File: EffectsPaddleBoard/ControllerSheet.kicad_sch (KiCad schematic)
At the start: 21 parts, among them J1 Conn_01x03_Pin, J2 Conn_01x06_Pin, J4 Conn_01x04_Pin, SW1 SW_SPDT, SW2 SW_SPDT, SW3 SW_SPDT, U1 STM32F405RGTx, Y1 16MHz

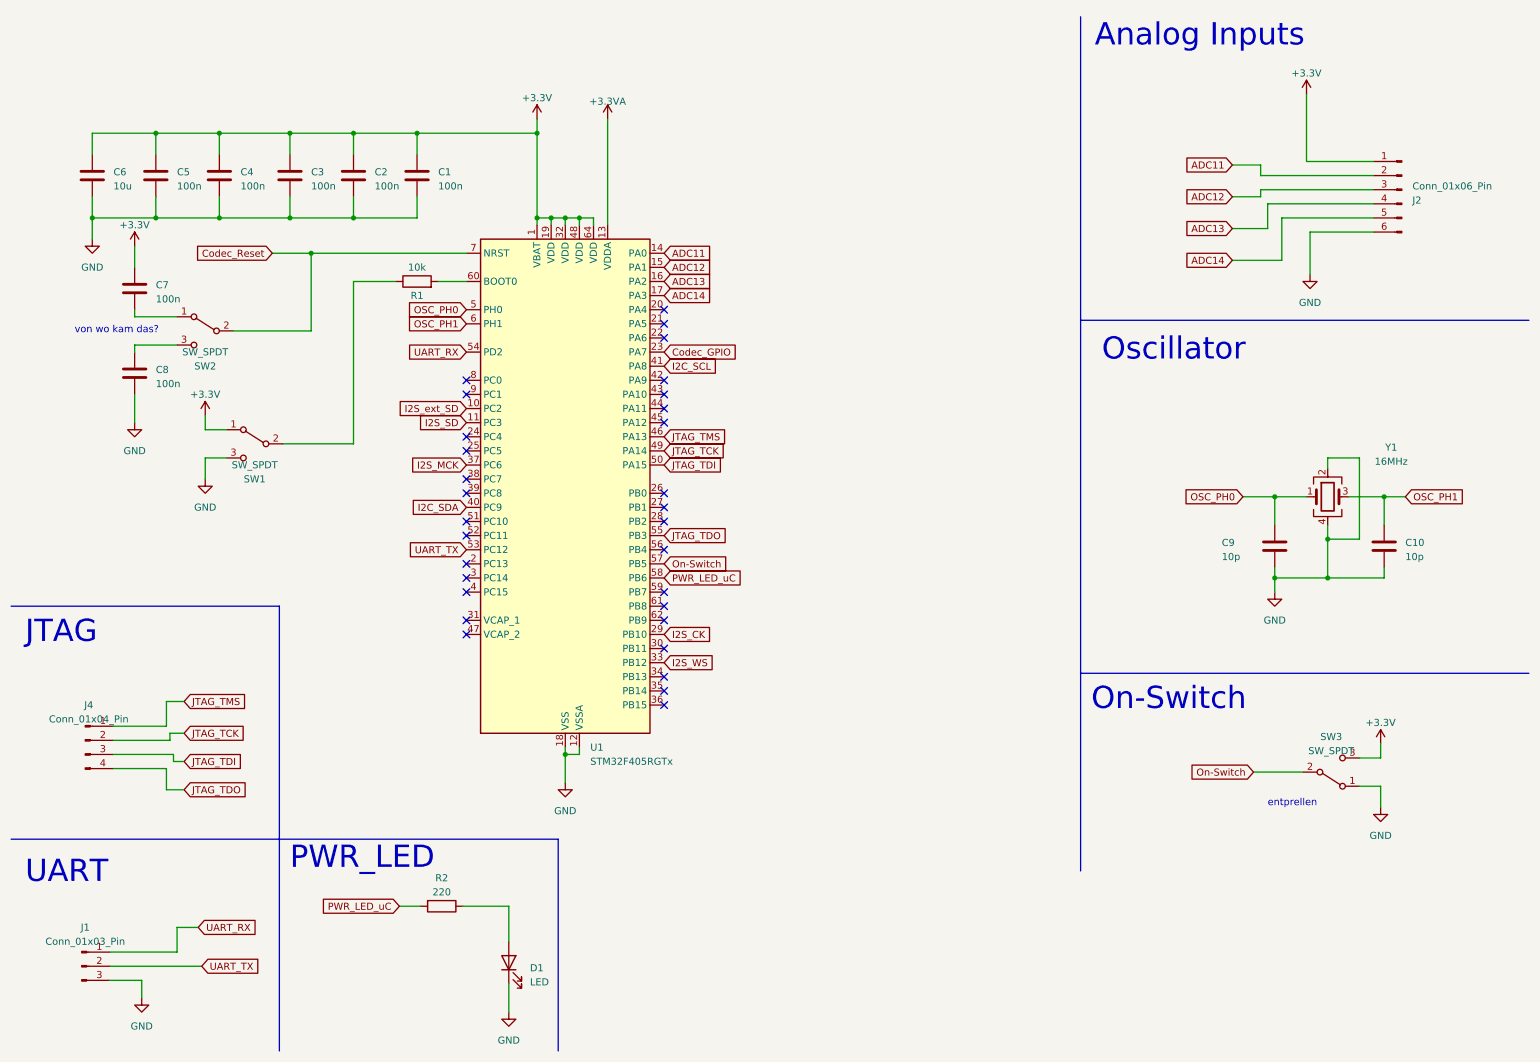
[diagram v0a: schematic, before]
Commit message: Added netclass colours and basic routing, made small changes in reset structure
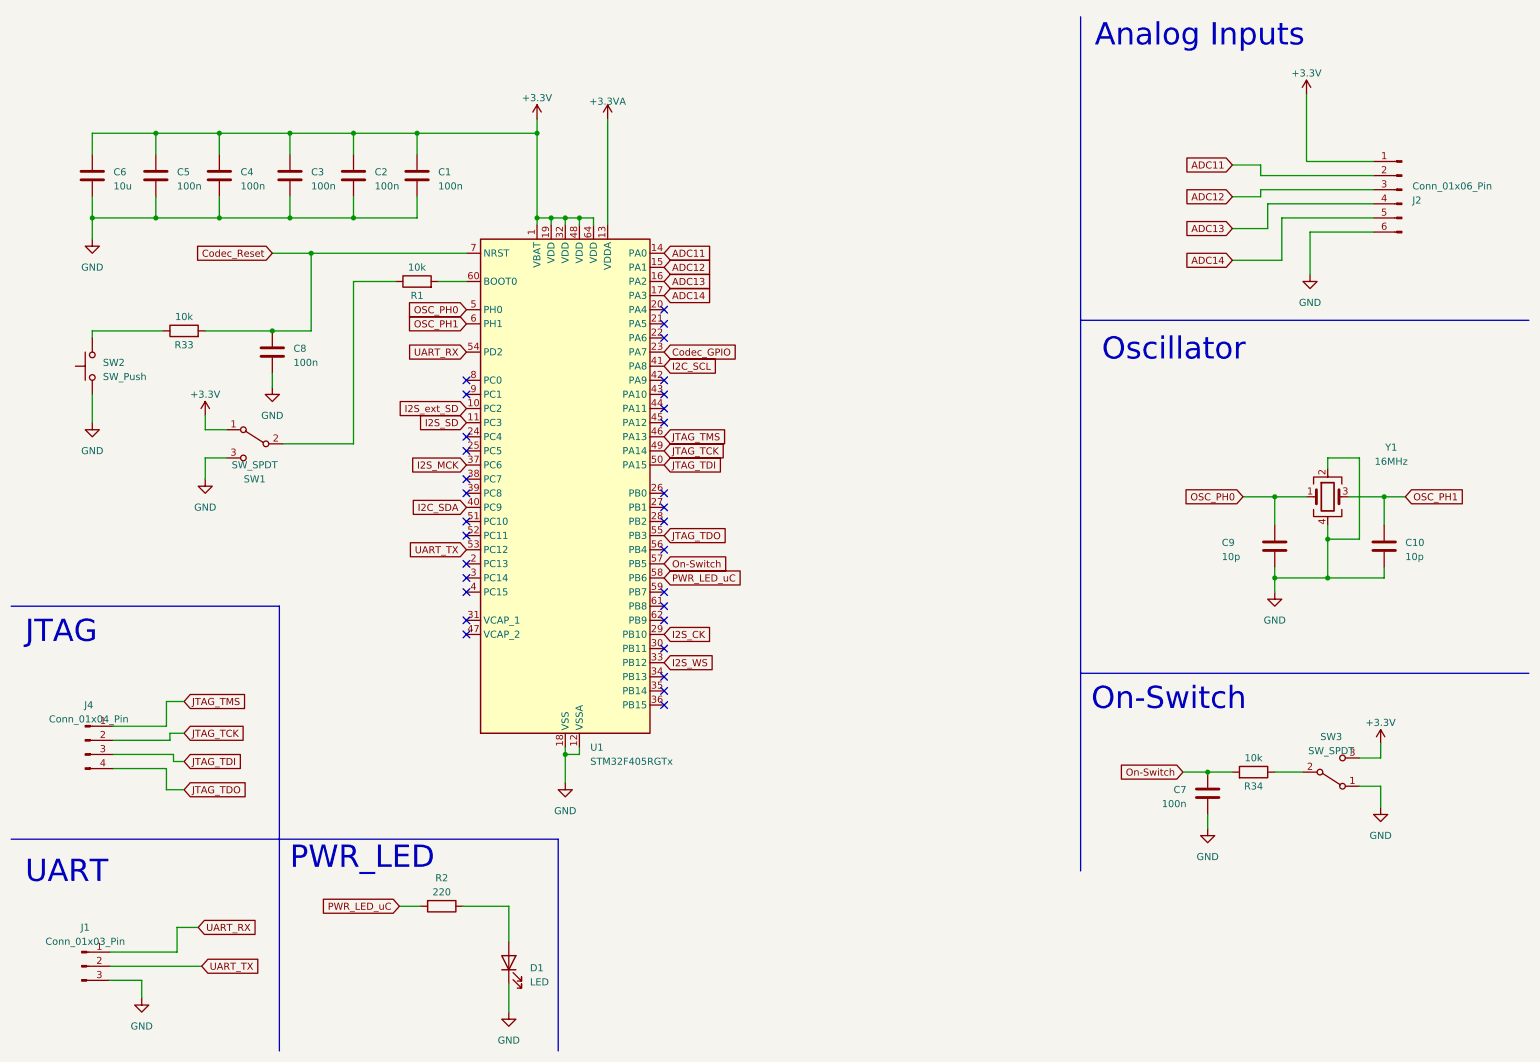
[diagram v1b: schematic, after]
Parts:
- removed SW2: SW_SPDT, Button_Switch_SMD:SW_SPDT_PCM12, symbol Switch:SW_SPDT
- added R33, R34: 10k, Resistor_SMD:R_0402_1005Metric, symbol Device:R
- added SW2: SW_Push, Button_Switch_SMD:SW_SPST_B3S-1000, symbol Switch:SW_Push
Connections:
- net +3.3V: no longer C7.1
- net Codec_Reset: now also C8.1, R33.2
- net GND: now also C7.2, SW2.1
- net On-Switch: now also C7.1, R34.2; no longer SW3.2 (B)
- new net: R33.1, SW2.2
- new net: R34.1, SW3.2 (B)
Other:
- note removed: "entprellen"
- note removed: "von wo kam das?"
- moved on the sheet: C8

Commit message: Tried separating analog and digital part
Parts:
- C1, C2, C3, C4, C5, C7, C8: Distributer Link (none) -> https://www.mouser.ch/ProductDetail/Murata-Electronics/GRM1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; Manufacturer (none) -> Murata Electronics; Manufacturer Part Number (none) -> GRM152R61A104KE19D
- C10, C9: Distributer Link (none) -> https://www.mouser.ch/ProductDetail/Murata-Electronics/GRM1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; Manufacturer (none) -> Murata Electronics; Manufacturer Part Number (none) -> GRM1555C1H100GA01D
- C6: Distributer Link (none) -> https://www.mouser.ch/ProductDetail/Murata-Electronics/GRM3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; Manufacturer (none) -> Murata Electronics; Manufacturer Part Number (none) -> GRM31CR71C106KAC7L
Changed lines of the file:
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@@
       (effects (font (size 1.27 1.27)) hide)
     )
-    (property "Distributer Link" "" (at 49.53 40.64 0)
-      (effects (font (size 1.27 1.27)) hide)
-    )
-    (property "Manufacturer" "" (at 49.53 40.64 0)
-      (effects (font (size 1.27 1.27)) hide)
-    )
-    (property "Manufacturer Part Number" "" (at 49.53 40.64 0)
+    (property "Distributer Link" "https://www.mouser.ch/ProductDetail/Murata-Electronics/GRM152R61A104KE19D?qs=IPQhFcwEUOjgOs7G%2Fz457g%3D%3D" (at 49.53 40.64 0)
+      (effects (font (size 1.27 1.27)) hide)
+    )
+    (property "Manufacturer" "Murata Electronics" (at 49.53 40.64 0)
+      (effects (font (size 1.27 1.27)) hide)
+    )
+    (property "Manufacturer Part Number" "GRM152R61A104KE19D" (at 49.53 40.64 0)
       (effects (font (size 1.27 1.27)) hide)
     )
@@
       (effects (font (size 1.27 1.27)) hide)
     )
-    (property "Distributer Link" "" (at 38.1 40.64 0)
-      (effects (font (size 1.27 1.27)) hide)
-    )
-    (property "Manufacturer" "" (at 38.1 40.64 0)
-      (effects (font (size 1.27 1.27)) hide)
-    )
-    (property "Manufacturer Part Number" "" (at 38.1 40.64 0)
+    (property "Distributer Link" "https://www.mouser.ch/ProductDetail/Murata-Electronics/GRM152R61A104KE19D?qs=IPQhFcwEUOjgOs7G%2Fz457g%3D%3D" (at 38.1 40.64 0)
+      (effects (font (size 1.27 1.27)) hide)
+    )
+    (property "Manufacturer" "Murata Electronics" (at 38.1 40.64 0)
+      (effects (font (size 1.27 1.27)) hide)
+    )
+    (property "Manufacturer Part Number" "GRM152R61A104KE19D" (at 38.1 40.64 0)
       (effects (font (size 1.27 1.27)) hide)
     )
@@
       (effects (font (size 1.27 1.27)) hide)
     )
-    (property "Distributer Link" "" (at 59.055 72.39 0)
-      (effects (font (size 1.27 1.27)) hide)
-    )
-    (property "Manufacturer" "" (at 59.055 72.39 0)
-      (effects (font (size 1.27 1.27)) hide)
-    )
-    (property "Manufacturer Part Number" "" (at 59.055 72.39 0)
+    (property "Distributer Link" "https://www.mouser.ch/ProductDetail/Murata-Electronics/GRM152R61A104KE19D?qs=IPQhFcwEUOjgOs7G%2Fz457g%3D%3D" (at 59.055 72.39 0)
+      (effects (font (size 1.27 1.27)) hide)
+    )
+    (property "Manufacturer" "Murata Electronics" (at 59.055 72.39 0)
+      (effects (font (size 1.27 1.27)) hide)
+    )
+    (property "Manufacturer Part Number" "GRM152R61A104KE19D" (at 59.055 72.39 0)
       (effects (font (size 1.27 1.27)) hide)
     )
@@
       (effects (font (size 1.27 1.27)) hide)
     )
-    (property "Distributer Link" "" (at 227.33 151.765 0)
-      (effects (font (size 1.27 1.27)) hide)
-    )
-    (property "Manufacturer" "" (at 227.33 151.765 0)
-      (effects (font (size 1.27 1.27)) hide)
-    )
-    (property "Manufacturer Part Number" "" (at 227.33 151.765 0)
+    (property "Distributer Link" "https://www.mouser.ch/ProductDetail/Murata-Electronics/GRM152R61A104KE19D?qs=IPQhFcwEUOjgOs7G%2Fz457g%3D%3D" (at 227.33 151.765 0)
+      (effects (font (size 1.27 1.27)) hide)
+    )
+    (property "Manufacturer" "Murata Electronics" (at 227.33 151.765 0)
+      (effects (font (size 1.27 1.27)) hide)
+    )
+    (property "Manufacturer Part Number" "GRM152R61A104KE19D" (at 227.33 151.765 0)
       (effects (font (size 1.27 1.27)) hide)
     )
@@
       (effects (font (size 1.27 1.27)) hide)
     )
-    (property "Distributer Link" "" (at 62.23 40.64 0)
-      (effects (font (size 1.27 1.27)) hide)
-    )
-    (property "Manufacturer" "" (at 62.23 40.64 0)
-      (effects (font (size 1.27 1.27)) hide)
-    )
-    (property "Manufacturer Part Number" "" (at 62.23 40.64 0)
+    (property "Distributer Link" "https://www.mouser.ch/ProductDetail/Murata-Electronics/GRM152R61A104KE19D?qs=IPQhFcwEUOjgOs7G%2Fz457g%3D%3D" (at 62.23 40.64 0)
+      (effects (font (size 1.27 1.27)) hide)
+    )
+    (property "Manufacturer" "Murata Electronics" (at 62.23 40.64 0)
+      (effects (font (size 1.27 1.27)) hide)
+    )
+    (property "Manufacturer Part Number" "GRM152R61A104KE19D" (at 62.23 40.64 0)
       (effects (font (size 1.27 1.27)) hide)
     )
@@
       (effects (font (size 1.27 1.27)) hide)
     )
-    (property "Distributer Link" "" (at 259.08 107.315 0)
-      (effects (font (size 1.27 1.27)) hide)
-    )
-    (property "Manufacturer" "" (at 259.08 107.315 0)
-      (effects (font (size 1.27 1.27)) hide)
-    )
-    (property "Manufacturer Part Number" "" (at 259.08 107.315 0)
+    (property "Distributer Link" "https://www.mouser.ch/ProductDetail/Murata-Electronics/GRM1555C1H100GA01D?qs=ouTquLLW2S7d2foNxe9pRA%3D%3D" (at 259.08 107.315 0)
+      (effects (font (size 1.27 1.27)) hide)
+    )
+    (property "Manufacturer" "Murata Electronics" (at 259.08 107.315 0)
+      (effects (font (size 1.27 1.27)) hide)
+    )
+    (property "Manufacturer Part Number" "GRM1555C1H100GA01D" (at 259.08 107.315 0)
       (effects (font (size 1.27 1.27)) hide)
     )
@@
       (effects (font (size 1.27 1.27)) hide)
     )
-    (property "Distributer Link" "" (at 73.66 40.64 0)
-      (effects (font (size 1.27 1.27)) hide)
-    )
-    (property "Manufacturer" "" (at 73.66 40.64 0)
-      (effects (font (size 1.27 1.27)) hide)
-    )
-    (property "Manufacturer Part Number" "" (at 73.66 40.64 0)
+    (property "Distributer Link" "https://www.mouser.ch/ProductDetail/Murata-Electronics/GRM152R61A104KE19D?qs=IPQhFcwEUOjgOs7G%2Fz457g%3D%3D" (at 73.66 40.64 0)
+      (effects (font (size 1.27 1.27)) hide)
+    )
+    (property "Manufacturer" "Murata Electronics" (at 73.66 40.64 0)
+      (effects (font (size 1.27 1.27)) hide)
+    )
+    (property "Manufacturer Part Number" "GRM152R61A104KE19D" (at 73.66 40.64 0)
       (effects (font (size 1.27 1.27)) hide)
     )
@@
       (effects (font (size 1.27 1.27)) hide)
     )
-    (property "Distributer Link" "" (at 239.395 107.315 0)
-      (effects (font (size 1.27 1.27)) hide)
-    )
-    (property "Manufacturer" "" (at 239.395 107.315 0)
-      (effects (font (size 1.27 1.27)) hide)
-    )
-    (property "Manufacturer Part Number" "" (at 239.395 107.315 0)
+    (property "Distributer Link" "https://www.mouser.ch/ProductDetail/Murata-Electronics/GRM1555C1H100GA01D?qs=ouTquLLW2S7d2foNxe9pRA%3D%3D" (at 239.395 107.315 0)
+      (effects (font (size 1.27 1.27)) hide)
+    )
+    (property "Manufacturer" "Murata Electronics" (at 239.395 107.315 0)
+      (effects (font (size 1.27 1.27)) hide)
+    )
+    (property "Manufacturer Part Number" "GRM1555C1H100GA01D" (at 239.395 107.315 0)
       (effects (font (size 1.27 1.27)) hide)
     )
@@
       (effects (font (size 1.27 1.27)) hide)
     )
-    (property "Distributer Link" "" (at 26.67 40.64 0)
-      (effects (font (size 1.27 1.27)) hide)
-    )
-    (property "Manufacturer" "" (at 26.67 40.64 0)
-      (effects (font (size 1.27 1.27)) hide)
-    )
-    (property "Manufacturer Part Number" "" (at 26.67 40.64 0)
+    (property "Distributer Link" "https://www.mouser.ch/ProductDetail/Murata-Electronics/GRM31CR71C106KAC7L?qs=jBEfVVNFvw7shEf0JgnbkQ%3D%3D" (at 26.67 40.64 0)
+      (effects (font (size 1.27 1.27)) hide)
+    )
+    (property "Manufacturer" "Murata Electronics" (at 26.67 40.64 0)
+      (effects (font (size 1.27 1.27)) hide)
+    )
+    (property "Manufacturer Part Number" "GRM31CR71C106KAC7L" (at 26.67 40.64 0)
       (effects (font (size 1.27 1.27)) hide)
     )
@@
       (effects (font (size 1.27 1.27)) hide)
     )
-    (property "Distributer Link" "" (at 85.09 40.64 0)
-      (effects (font (size 1.27 1.27)) hide)
-    )
-    (property "Manufacturer" "" (at 85.09 40.64 0)
-      (effects (font (size 1.27 1.27)) hide)
-    )
-    (property "Manufacturer Part Number" "" (at 85.09 40.64 0)
-      (effects (font (size 1.27 1.27)) hide)
-    )
+    (property "Distributer Link" "https://www.mouser.ch/ProductDetail/Murata-Electronics/GRM152R61A104KE19D?qs=IPQhFcwEUOjgOs7G%2Fz457g%3D%3D" (at 85.09 40.64 0)
+      (effects (font (size 1.27 1.27)) hide)
+    )
+    (property "Manufacturer" "Murata Electronics" (at 85.09 40.64 0)
+      (effects (font (size 1.27 1.27)) hide)
+    )
+    (property "Manufacturer Part Number" "GRM152R61A104KE19D" (at 85.09 40.64 0)
+      (effects (font (size 1.27 1.27)) hide)
+    )
